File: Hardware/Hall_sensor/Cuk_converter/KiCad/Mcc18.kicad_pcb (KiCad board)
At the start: 2 copper layers, 199.1 x 107.2 mm, 53 parts, among them Q1 IRFP4321PbF, U1 LTSP_25-NP, U2 DRIVER_(INEP), U3 LM7812_TO220, U4 Signals_MCC, U5 ZCS

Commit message: fixed and created all Fabrication files
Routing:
- added copper zone on B.Cu, net (none)
- added copper zone on F.Cu, net (none)
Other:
- board size 199.1 x 107.2 mm -> 199.1 x 117.9 mm
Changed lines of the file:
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@@
   (general
     (thickness 1.6)
-    (drawings 8)
+    (drawings 10)
     (tracks 553)
     (zones 0)
@@
     (user_trace_width 12)
     (trace_clearance 0.3048)
-    (zone_clearance 0.3048)
+    (zone_clearance 1.27)
     (zone_45_only no)
     (trace_min 0.508)
@@
       (padsonsilk false)
       (subtractmaskfromsilk true)
-      (outputformat 1)
+      (outputformat 4)
       (mirror false)
       (drillshape 0)
       (scaleselection 1)
-      (outputdirectory GERBERS/))
+      (outputdirectory PDF/))
   )
   (net 0 "")
@@
     )
   )
+  (gr_line (start 249.174 147.066) (end 249.174 152.4) (layer Edge.Cuts) (width 0.15))
+  (gr_line (start 50.038 147.066) (end 50.038 152.4) (layer Edge.Cuts) (width 0.15))
+  (gr_line (start 50.038 39.878) (end 50.038 34.544) (layer Edge.Cuts) (width 0.15))
+  (gr_line (start 249.174 39.878) (end 249.174 34.544) (layer Edge.Cuts) (width 0.15))
   (gr_line (start 50.038 147.066) (end 50.038 39.878) (layer Edge.Cuts) (width 0.15))
-  (gr_line (start 249.174 147.066) (end 50.038 147.066) (layer Edge.Cuts) (width 0.15))
+  (gr_line (start 249.174 152.4) (end 50.038 152.4) (layer Edge.Cuts) (width 0.15))
   (gr_line (start 249.174 39.878) (end 249.174 147.066) (layer Edge.Cuts) (width 0.15))
-  (gr_line (start 50.038 39.878) (end 249.174 39.878) (layer Edge.Cuts) (width 0.15))
-  (dimension 202.184 (width 0.3) (layer Dwgs.User)
-    (gr_text "7.9600 in" (at 151.13 155.262) (layer Dwgs.User)
-      (effects (font (size 1.5 1.5) (thickness 0.3)))
-    )
-    (feature1 (pts (xy 252.222 147.066) (xy 252.222 153.748421)))
-    (feature2 (pts (xy 50.038 147.066) (xy 50.038 153.748421)))
-    (crossbar (pts (xy 50.038 153.162) (xy 252.222 153.162)))
-    (arrow1a (pts (xy 252.222 153.162) (xy 251.095496 153.748421)))
-    (arrow1b (pts (xy 252.222 153.162) (xy 251.095496 152.575579)))
-    (arrow2a (pts (xy 50.038 153.162) (xy 51.164504 153.748421)))
-    (arrow2b (pts (xy 50.038 153.162) (xy 51.164504 152.575579)))
-  )
-  (dimension 202.18416 (width 0.3) (layer Dwgs.User)
-    (gr_text "202.184 mm" (at 151.148273 161.738339 0.07197958464) (layer Dwgs.User)
-      (effects (font (size 1.5 1.5) (thickness 0.3)))
-    )
-    (feature1 (pts (xy 50.038 147.32) (xy 50.054372 160.351761)))
-    (feature2 (pts (xy 252.222 147.066) (xy 252.238372 160.097761)))
-    (crossbar (pts (xy 252.237635 159.511341) (xy 50.053635 159.765341)))
-    (arrow1a (pts (xy 50.053635 159.765341) (xy 51.179401 159.177506)))
-    (arrow1b (pts (xy 50.053635 159.765341) (xy 51.180875 160.350346)))
-    (arrow2a (pts (xy 252.237635 159.511341) (xy 251.110395 158.926336)))
-    (arrow2b (pts (xy 252.237635 159.511341) (xy 251.111869 160.099176)))
-  )
+  (gr_line (start 50.038 34.544) (end 249.174 34.544) (layer Edge.Cuts) (width 0.15))
   (dimension 107.188301 (width 0.3) (layer Dwgs.User)
     (gr_text "4.2200 in" (at 41.211258 93.493217 270.1357717) (layer Dwgs.User)
@@
   (segment (start 127.82136 51.8541) (end 129.21736 50.4581) (width 0.635) (layer F.Cu) (net 60) (status 40000))
   (zone (net 39) (net_name /Source) (layer B.Cu) (hatch edge 0.508)
-    (priority 1)
+    (priority 2)
     (connect_pads yes (clearance 1.27))
     (min_thickness 0.508)
@@
   )
   (zone (net 41) (net_name GND) (layer B.Cu) (hatch edge 0.508)
+    (priority 1)
     (connect_pads yes (clearance 0.3048))
     (min_thickness 0.508)
@@
   )
   (zone (net 48) (net_name /+B) (layer B.Cu) (hatch edge 0.508)
-    (priority 2)
+    (priority 8)
     (connect_pads yes (clearance 1.27))
     (min_thickness 0.508)
@@
   )
   (zone (net 37) (net_name /+Vp) (layer B.Cu) (hatch edge 0.508)
-    (priority 2)
+    (priority 5)
     (connect_pads yes (clearance 1.27))
     (min_thickness 0.508)
@@
   )
   (zone (net 48) (net_name /+B) (layer F.Cu) (hatch edge 0.508)
+    (priority 8)
     (connect_pads yes (clearance 1.27))
     (min_thickness 0.508)
@@
       )
     )
+  )
+  (zone (net 0) (net_name "") (layer F.Cu) (hatch edge 0.508)
+    (connect_pads yes (clearance 1.27))
+    (min_thickness 0.508)
+    (fill yes (arc_segments 16) (thermal_gap 0.508) (thermal_bridge_width 0.508))
+    (polygon
+      (pts
+        (xy 50.038 34.544) (xy 249.174 34.544) (xy 249.174 39.878) (xy 50.038 39.878)
+      )
+    )
+  )
+  (zone (net 0) (net_name "") (layer B.Cu) (hatch edge 0.508)
+    (connect_pads yes (clearance 1.27))
+    (min_thickness 0.508)
+    (fill yes (arc_segments 16) (thermal_gap 0.508) (thermal_bridge_width 0.508))
+    (polygon
+      (pts
+        (xy 50.038 34.544) (xy 249.174 34.544) (xy 249.174 39.878) (xy 50.038 39.878)
+      )
+    )
+  )
+  (zone (net 0) (net_name "") (layer F.Cu) (hatch edge 0.508)
+    (connect_pads yes (clearance 1.27))
+    (min_thickness 0.508)
+    (fill yes (arc_segments 16) (thermal_gap 0.508) (thermal_bridge_width 0.508))
+    (polygon
+      (pts
+        (xy 249.174 147.066) (xy 249.174 152.4) (xy 50.038 152.4) (xy 50.038 147.066)
+      )
+    )
+  )
+  (zone (net 0) (net_name "") (layer B.Cu) (hatch edge 0.508)
+    (connect_pads yes (clearance 1.27))
+    (min_thickness 0.508)
+    (fill yes (arc_segments 16) (thermal_gap 0.508) (thermal_bridge_width 0.508))
+    (polygon
+      (pts
+        (xy 249.174 147.066) (xy 249.174 152.4) (xy 50.038 152.4) (xy 50.038 147.066)
+      )
+    )

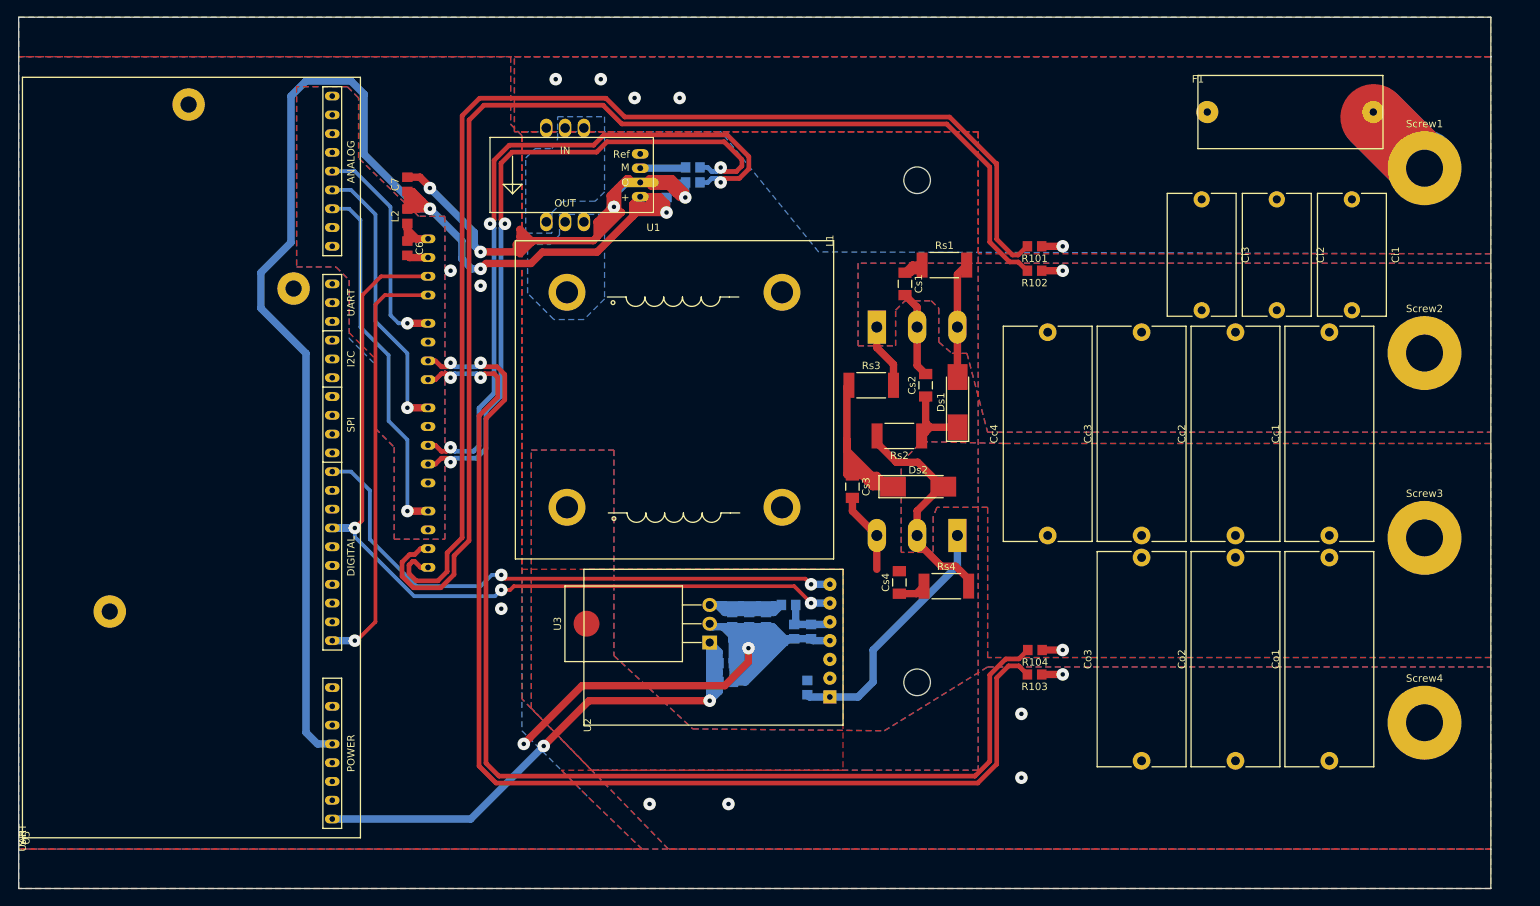
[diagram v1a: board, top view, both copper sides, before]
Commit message: Added trak between Shunt and Inductor
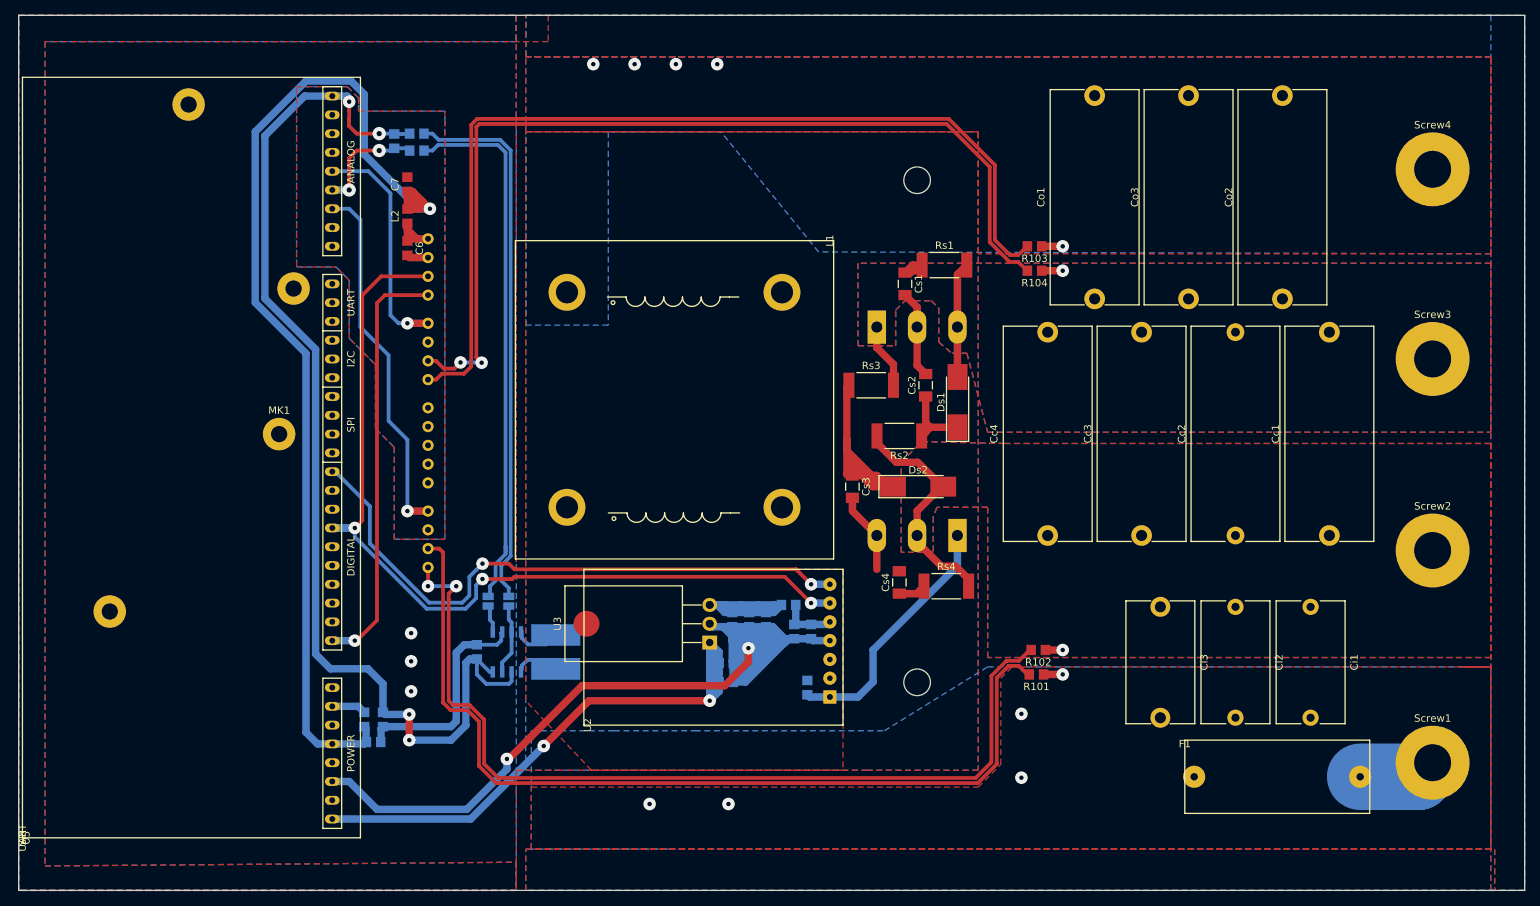
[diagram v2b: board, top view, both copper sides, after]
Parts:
- removed R106: 0R, Resistor_SMD:R_0805_2012Metric_Pad1.29x1.40mm_HandSolder
- added C11: 100nF, MCCplaca Shunt:C_0805_2012Metric_Pad1.29x1.40mm_HandSolder, B.Cu at (112.0, 120.4)
- added C12: 100nF, MCC:C_0805_2012Metric_Pad1.29x1.40mm_HandSolder, B.Cu at (99.3, 129.5)
- added C13: 100nF, MCC:C_0805_2012Metric_Pad1.29x1.40mm_HandSolder, B.Cu at (96.8, 129.5)
- added L4: L_Small, Inductor_SMD:L_0805_2012Metric_Pad1.29x1.40mm_HandSolder, B.Cu at (98.0, 132.6)
- added MK1: Mounting_Hole, MountingHole:MountingHole_2.2mm_M2_Pad, F.Cu at (85.3, 90.9)
- added R107: 0R, Jumper:SolderJumper-2_P1.3mm_Open_Pad1.0x1.5mm, B.Cu at (116.3, 113.5)
- added R109: ??, Resistor_SMD:R_0805_2012Metric_Pad1.29x1.40mm_HandSolder, B.Cu at (103.9, 50.3)
- added R110: ??, Resistor_SMD:R_0805_2012Metric_Pad1.29x1.40mm_HandSolder, B.Cu at (103.9, 52.6)
- added Rshunt1: 500uR, MCCplaca Shunt:PML100HZPJV0L5, B.Cu at (122.7, 120.4)
- C1: footprint MCC:C_0805_2012Metric_Pad1.29x1.40mm_HandSolder -> MCCplaca Shunt:C_0805_2012Metric_Pad1.29x1.40mm_HandSolder
- R105: footprint Resistor_SMD:R_0805_2012Metric_Pad1.29x1.40mm_HandSolder -> Jumper:SolderJumper-2_P1.3mm_Open_Pad1.0x1.5mm
- U1: value LTSP_25-NP -> INA240; footprint MCCplaca:LTSP_25-NP -> Package_SO:SOIC-8_3.9x4.9mm_P1.27mm; moved to B.Cu
- moved F1 89.9 mm to (207.8, 132.3)
- moved Screw1 80.4 mm to (241.3, 135.4)
- moved Screw4 74.9 mm to (241.3, 55.1)
- moved Co1 70.1 mm to (195.6, 72.6)
- moved R105 64.9 mm to (113.5, 113.5), turned to 90 degrees
- moved Co2 62.8 mm to (221.0, 72.6)
- moved Co3 62.8 mm to (208.3, 72.6)
- moved U1 62.7 mm to (116.1, 120.4), turned to 90 degrees
- moved R101 57.9 mm to (187.7, 123.4)
- moved R103 57.9 mm to (187.5, 65.5)
- moved Ci1 55.4 mm to (224.8, 114.3)
- moved Ci2 55.4 mm to (214.6, 114.3)
- moved Ci3 55.4 mm to (204.5, 114.3)
- moved R102 51.3 mm to (188.0, 120.1)
- moved R104 51.3 mm to (187.5, 68.8)
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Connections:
- C1 pad 1: GND -> /Ipanel_adc+
- C1 pad 2: +5V -> GNDA
- Cc1 pad 1: /-B -> /+Vp
- Cc1 pad 2: /+Vp -> /-B
- Cc2 pad 1: /-B -> /+Vp
- Cc2 pad 2: /+Vp -> /-B
- Cc3 pad 1: /-B -> /+Vp
- Cc3 pad 2: /+Vp -> /-B
- Cc4 pad 1: /-B -> /+Vp
- Cc4 pad 2: /+Vp -> /-B
- Ci1 pad 1: /-Vp -> /+Vp
- Ci1 pad 2: /+Vp -> /-Vp
- Ci2 pad 1: /-Vp -> /+Vp
- Ci2 pad 2: /+Vp -> /-Vp
- Ci3 pad 1: /-Vp -> /+Vp
- Ci3 pad 2: /+Vp -> /-Vp
- Co1 pad 1: /+B -> /-B
- Co1 pad 2: /-B -> /+B
- Co2 pad 1: /+B -> /-B
- Co2 pad 2: /-B -> /+B
- Co3 pad 1: /+B -> /-B
- Co3 pad 2: /-B -> /+B
- D1 pad 1: /+Vp -> /-B
- D1 pad 3: /+Vp -> /-B
- Ds1 pad 2: /+Vp -> /-B
- Ds2 pad 2: /-B -> /+Vp
- L1 pad 1: Net-(L1-Pad1) -> /+B
- L1 pad 3: /+B -> /Rs+
- Q1 pad 2: /-B -> /+Vp
- R105 pad 1: /+Ip -> /INA240_OUT
- Rs1 pad 2: /+Vp -> /-B
- Rs2 pad 2: /-B -> /+Vp
- Rs3 pad 2: /+Vp -> /-B
- Rs4 pad 2: /-B -> /+Vp
- U1 pad 1: Net-(L1-Pad1) -> /-Vp
- U1 pad 2: Net-(L1-Pad1) -> GNDA
- U1 pad 3: Net-(U1-Pad3) -> GNDA
- U1 pad 4: /-Vp -> GNDA
- U1 pad 5: Net-(U1-Pad3) -> /INA240_OUT
- U1 pad 6: Net-(U1-Pad3) -> +5VA
- U1 pad 7: +5V -> GNDA
- U1 pad 8: GND -> /Rs+
- U4 pad 6: /Ip_sen+ -> Net-(U4-Pad6)
- U4 pad 7: /Ip_sen- -> Net-(U4-Pad7)
- U4 pad 8: GNDA -> Net-(U4-Pad8)
- U4 pad 9: /Ipanel_adc+ -> Net-(U4-Pad9)
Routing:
- net GNDA: track 2.92 -> 163.7 mm, vias 0 -> 4
- net GND: track 315.1 -> 255.4 mm, vias 11 -> 7
- net +5V: track 200.1 -> 147.3 mm, vias 3 -> 1
- net /Vp_sen+: track 168.6 -> 123.5 mm
- net /Vp_sen-: track 166.0 -> 123.7 mm, vias 0 -> 2
- net +5VA: track 7.91 -> 37.6 mm
- net /Vb_sen+: track 153.5 -> 128.9 mm, vias 2 -> 0
- net /Vb_sen-: track 153.6 -> 130.0 mm
- net /Ipanel_adc+: track 38.0 -> 14.9 mm, vias 1 -> 2
- net /Ip_sen-: track 94.5 -> 74.0 mm, vias 3 -> 0
- net /Ip_sen+: track 91.3 -> 73.4 mm, vias 3 -> 0
- net /-P_unfused: track 19.8 -> 10.6 mm
- net /-B: track 33.9 -> 26.8 mm
- net /+Vp: track 26.8 -> 33.9 mm
- net /Rs+: track 0.00 -> 6.39 mm
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- removed copper zone on B.Cu, net Net-(L1-Pad1)
- removed copper zone on B.Cu, net Net-(U1-Pad3)
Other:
- board size 199.1 x 117.9 mm -> 203.7 x 118.4 mm
- net class INA added: clearance 0.3048, trace_width 0.3429, via_dia 0.9, via_drill 0.7
- rule trace_min: 0.508 -> 0.3429

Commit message: Fixing the Hall_Cuk
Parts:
- removed C11: 100nF, MCCplaca Shunt:C_0805_2012Metric_Pad1.29x1.40mm_HandSolder
- removed C12, C13: 100nF, MCC:C_0805_2012Metric_Pad1.29x1.40mm_HandSolder
- removed L4: L_Small, Inductor_SMD:L_0805_2012Metric_Pad1.29x1.40mm_HandSolder
- removed MK1: Mounting_Hole, MountingHole:MountingHole_2.2mm_M2_Pad
- removed R107: 0R, Jumper:SolderJumper-2_P1.3mm_Open_Pad1.0x1.5mm
- removed R109, R110: ??, Resistor_SMD:R_0805_2012Metric_Pad1.29x1.40mm_HandSolder
- removed Rshunt1: 500uR, MCCplaca Shunt:PML100HZPJV0L5
- added R106: 0R, Resistor_SMD:R_0805_2012Metric_Pad1.29x1.40mm_HandSolder, B.Cu at (115.6, 97.5)
- C1: footprint MCCplaca Shunt:C_0805_2012Metric_Pad1.29x1.40mm_HandSolder -> MCC:C_0805_2012Metric_Pad1.29x1.40mm_HandSolder
- R105: footprint Jumper:SolderJumper-2_P1.3mm_Open_Pad1.0x1.5mm -> Resistor_SMD:R_0805_2012Metric_Pad1.29x1.40mm_HandSolder
- U1: value INA240 -> LTSP_25-NP; footprint Package_SO:SOIC-8_3.9x4.9mm_P1.27mm -> MCCplaca:LTSP_25-NP
- moved U1 23.7 mm to (122.4, 143.3), turned to 0 degrees
- moved R105 16.0 mm to (113.3, 97.5)
- turned C1 to 270 degrees
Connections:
- net /-P_unfused renamed Net-(F1-Pad2)
- C1 pad 1: /Ipanel_adc+ -> GND
- C1 pad 2: GNDA -> +5V
- L1 pad 3: /Rs+ -> Net-(L1-Pad3)
- R105 pad 1: /INA240_OUT -> /+Ip
- U1 pad 1: /-Vp -> Net-(L1-Pad3)
- U1 pad 2: GNDA -> Net-(L1-Pad3)
- U1 pad 3: GNDA -> Net-(U1-Pad3)
- U1 pad 4: GNDA -> /-Vp
- U1 pad 5: /INA240_OUT -> Net-(U1-Pad3)
- U1 pad 6: +5VA -> Net-(U1-Pad3)
- U1 pad 7: GNDA -> +5V
- U1 pad 8: /Rs+ -> GND
- U4 pad 6: Net-(U4-Pad6) -> /Ip_sen+
- U4 pad 7: Net-(U4-Pad7) -> /Ip_sen-
- U4 pad 8: Net-(U4-Pad8) -> GNDA
- U4 pad 9: Net-(U4-Pad9) -> /Ipanel_adc+
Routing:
- net GND: track 255.4 -> 336.0 mm, vias 7 -> 9
- net /Ip_sen+: track 73.4 -> 10.6 mm
- net /Ip_sen-: track 74.0 -> 13.1 mm
- net GNDA: track 163.7 -> 110.7 mm, vias 4 -> 2
- net /+Ip: track 0.00 -> 48.0 mm
- net +5VA: track 37.6 -> 7.91 mm
- net +5V: track 147.3 -> 176.8 mm
- net /Vp_sen+: track 123.5 -> 141.2 mm
- net /Vp_sen-: track 123.7 -> 141.2 mm
- net /Rs+: track 6.39 -> 0.00 mm
- net /-Vp: track 8.22 -> 2.36 mm, vias 5 -> 3
- net /INA240_OUT: track 3.67 -> 0.00 mm
- net /Ipanel_adc+: track 14.9 -> 12.7 mm
- net /+18V_OUT: track 84.0 -> 81.9 mm

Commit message: Fixed Errors
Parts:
- U1: moved to F.Cu
- moved C1 86.0 mm to (111.3, 136.7), turned to 90 degrees
- moved U1 14.2 mm to (112.3, 133.3)
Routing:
- net GNDA: track 110.7 -> 12.6 mm, vias 2 -> 0
- net GND: track 336.0 -> 321.2 mm
- net /Ipanel_adc+: track 12.7 -> 0.00 mm, vias 2 -> 0
- net +5V: track 176.8 -> 165.1 mm
- net /+18V_OUT: track 81.9 -> 88.4 mm
- net /Vb_sen-: track 130.0 -> 127.4 mm
- net /+Ip: track 48.0 -> 45.9 mm, vias 0 -> 2
- net /Vb_sen+: track 128.9 -> 127.1 mm
- net /Vp_sen+: track 141.2 -> 142.6 mm
- net /Vp_sen-: track 141.2 -> 142.4 mm, vias 2 -> 0
- net /-Vp: vias 3 -> 6
- added copper zone on B.Cu, net Net-(L1-Pad3)
- added copper zone on B.Cu, net Net-(U1-Pad3)
